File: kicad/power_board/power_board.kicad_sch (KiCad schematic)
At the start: 62 parts, among them J1 24V, J10 Grid, J11 24V Solar, J12 MCU_2, J13 GND, J2 24V, J3 GND, J4 GND, J5 GND, J6 GND, J7 MCU, J8 GND, J9 Solar Panel, Q1 FDD8453LZ, Q2 FDD8453LZ, Q3 FDD8453LZ, Q4 FDD8453LZ, Q5 FDS5670, U1 LTC4151xMS, U5 LT3757A, U6 LT1161

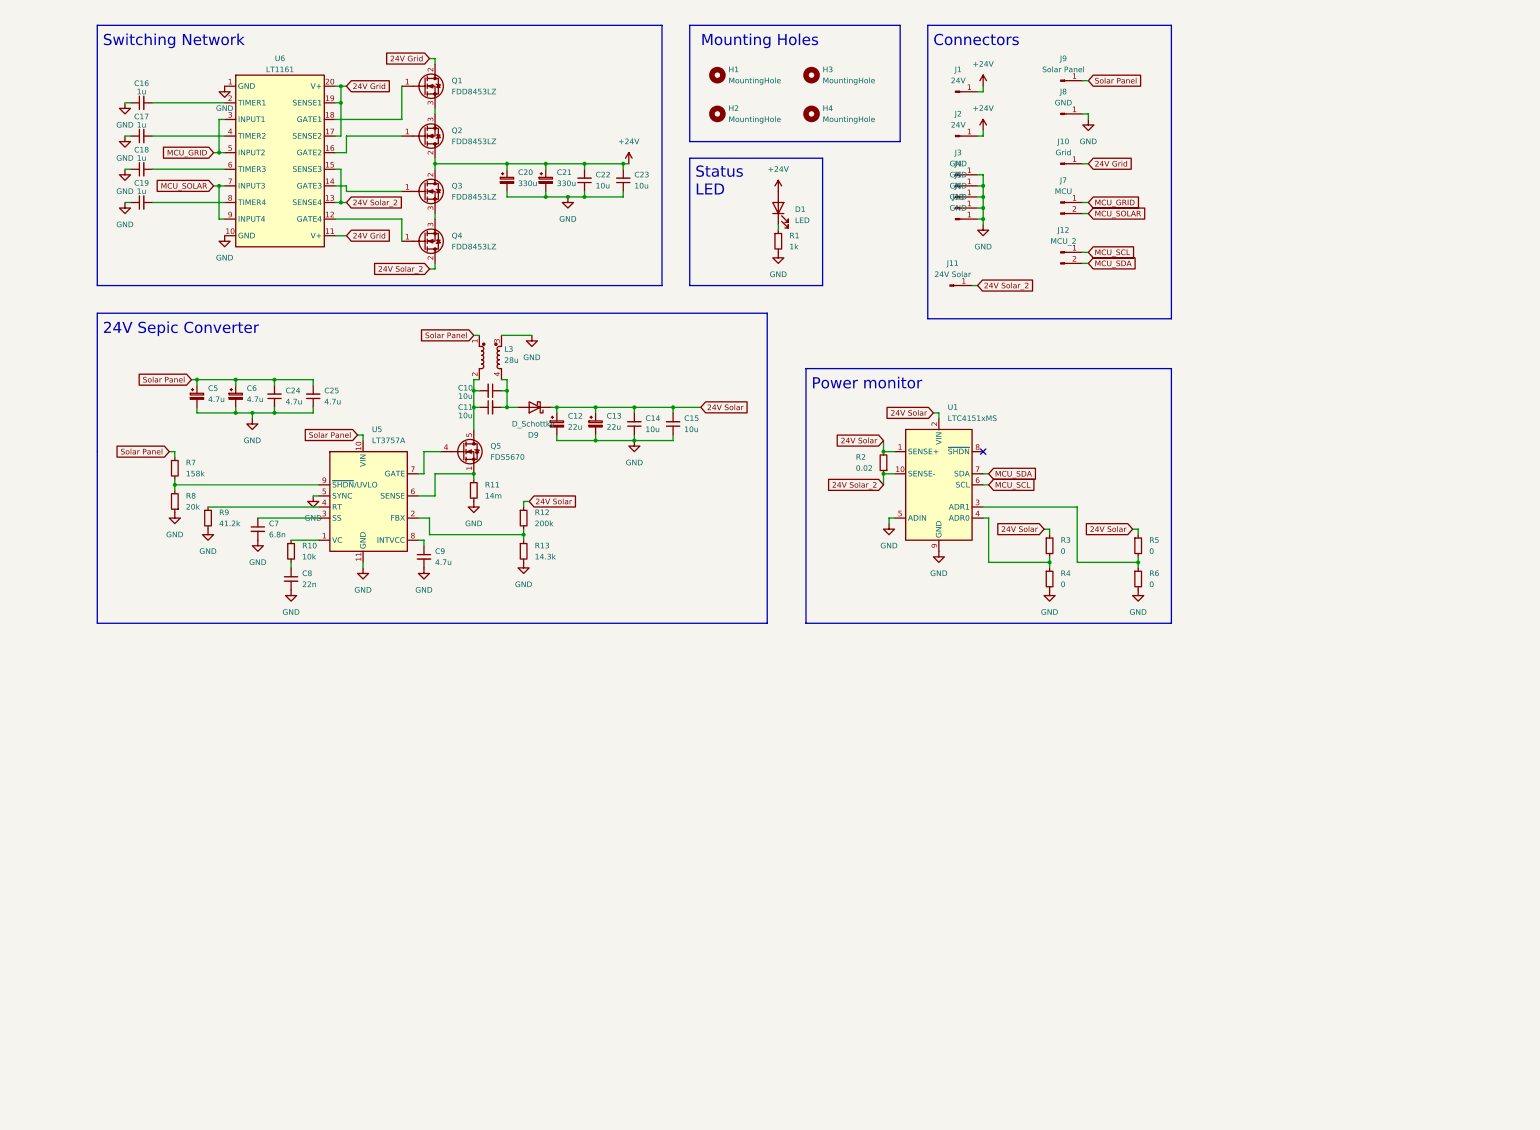
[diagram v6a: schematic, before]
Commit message: added isolation to power and light boards
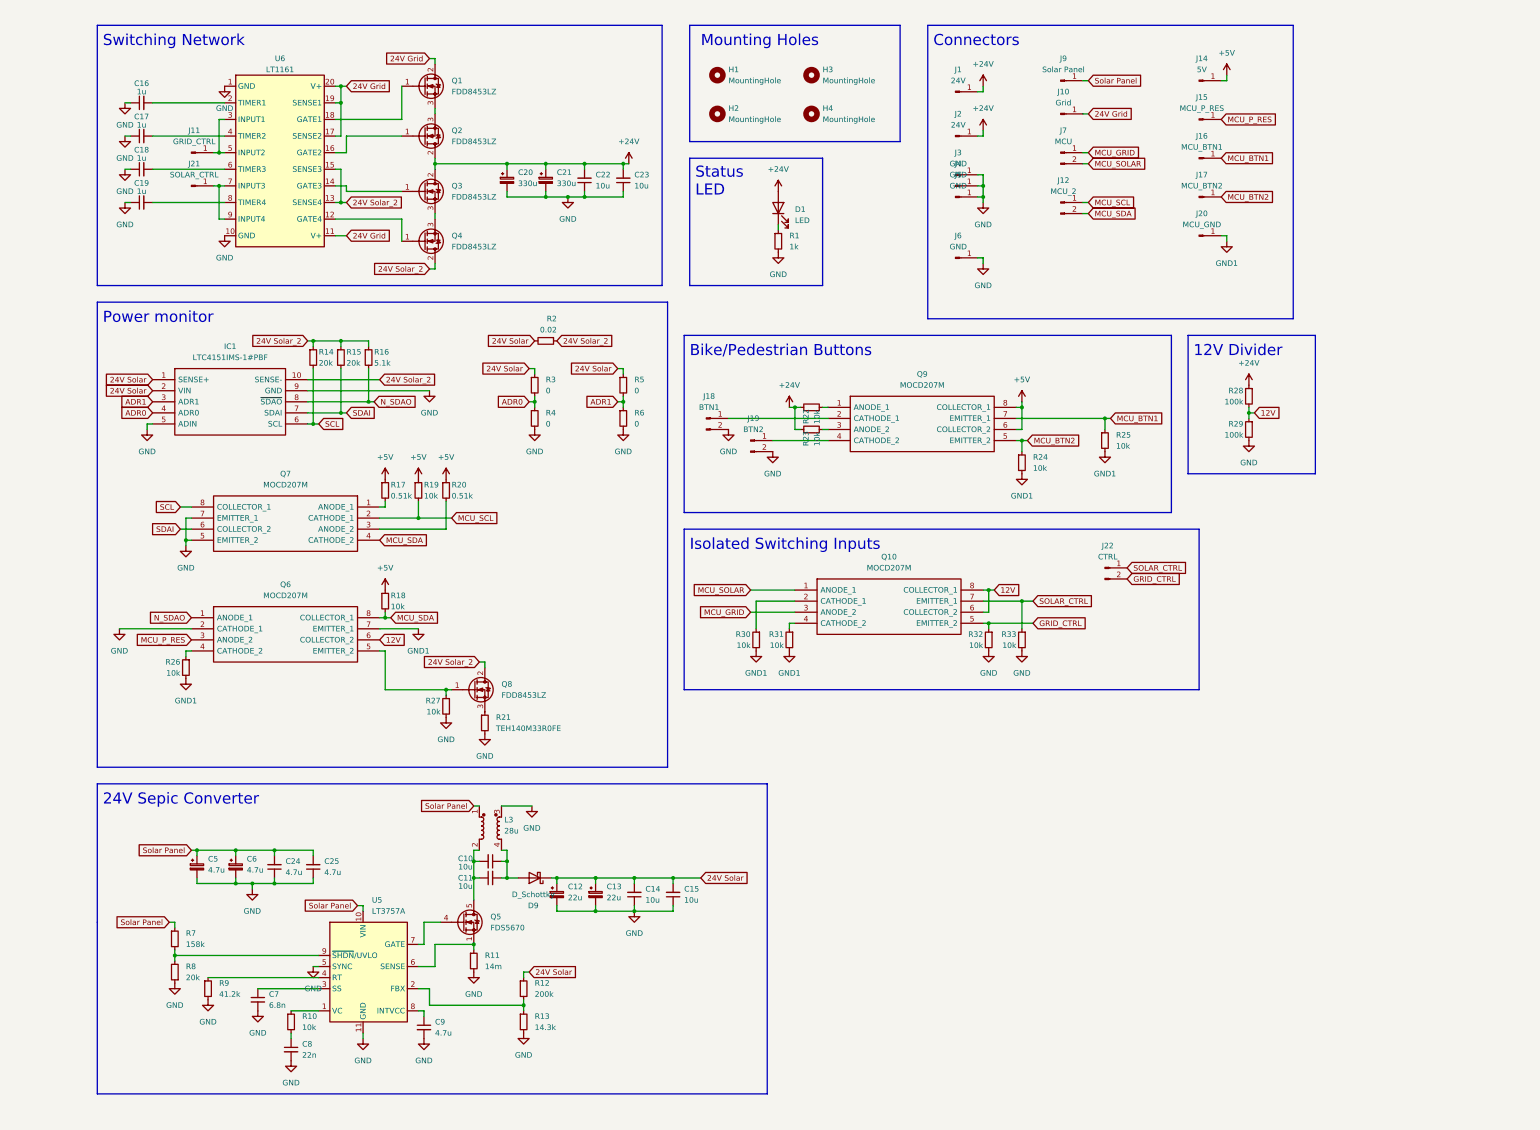
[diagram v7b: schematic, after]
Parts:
- removed J13: GND, Connector_PinHeader_2.54mm:PinHeader_1x01_P2.54mm_Vertical, symbol Connector:Conn_01x01_Male
- removed J8: GND, _mine:73099, symbol Connector:Conn_01x01_Male
- removed U1: LTC4151xMS, Package_SO:MSOP-10_3x3mm_P0.5mm, symbol Analog_ADC:LTC4151xMS
- added IC1: LTC4151IMS-1#PBF, Package_SO:MSOP-10_3x3mm_P0.5mm, symbol SamacSys_Parts:LTC4151IMS-1#PBF
- added J14: 5V, Connector_PinHeader_2.54mm:PinHeader_1x01_P2.54mm_Vertical, symbol Connector:Conn_01x01_Male
- added J15: MCU_P_RES, Connector_PinHeader_2.54mm:PinHeader_1x01_P2.54mm_Vertical, symbol Connector:Conn_01x01_Male
- added J16: MCU_BTN1, Connector_PinHeader_2.54mm:PinHeader_1x01_P2.54mm_Vertical, symbol Connector:Conn_01x01_Male
- added J17: MCU_BTN2, Connector_PinHeader_2.54mm:PinHeader_1x01_P2.54mm_Vertical, symbol Connector:Conn_01x01_Male
- added J18: BTN1, Connector_PinHeader_2.54mm:PinHeader_1x02_P2.54mm_Vertical, symbol Connector:Conn_01x02_Male
- added J19: BTN2, Connector_PinHeader_2.54mm:PinHeader_1x02_P2.54mm_Vertical, symbol Connector:Conn_01x02_Male
- added J20: MCU_GND, Connector_PinHeader_2.54mm:PinHeader_1x01_P2.54mm_Vertical, symbol Connector:Conn_01x01_Male
- added J21: SOLAR_CTRL, Connector_PinHeader_2.54mm:PinHeader_1x01_P2.54mm_Vertical, symbol Connector:Conn_01x01_Male
- added J22: CTRL, Connector_PinHeader_2.54mm:PinHeader_1x02_P2.54mm_Vertical, symbol Connector:Conn_01x02_Male
- added Q10, Q6, Q7, Q9: MOCD207M, Package_SO:SOIC-8_3.9x4.9mm_P1.27mm, symbol SamacSys_Parts:MOCD207M
- added Q8: FDD8453LZ, Package_TO_SOT_SMD:TO-252-2, symbol Transistor_FET:BSP89
- added R14, R15: 20k, Resistor_SMD:R_0603_1608Metric, symbol Device:R_Small
- added R16: 5.1k, Resistor_SMD:R_0603_1608Metric, symbol Device:R_Small
- added R17, R20: 0.51k, Resistor_SMD:R_0805_2012Metric, symbol Device:R_Small
- added R18, R19, R22, R23, R24, R25, R26, R27, R30, R31, R32, R33: 10k, Resistor_SMD:R_0805_2012Metric, symbol Device:R_Small
- added R21: TEH140M33R0FE, Resistor_THT:R_Axial_DIN0207_L6.3mm_D2.5mm_P10.16mm_Horizontal, symbol Device:R_Small
- added R28, R29: 100k, Resistor_SMD:R_1206_3216Metric, symbol Device:R_Small
- J11: value 24V Solar -> GRID_CTRL
- J6: footprint Connector_PinHeader_2.54mm:PinHeader_1x01_P2.54mm_Vertical -> _mine:73099
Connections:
- net +24V: now also R22.1, R23.1, R28.1
- net 24V Solar: now also IC1.1 (SENSE+), IC1.2 (VIN)
- net 24V Solar_2: now also IC1.10 (SENSE-), Q8.2 (D), R14.1, R15.1, R16.1; no longer J11.1 (Pin_1)
- net GND: now also IC1.5 (ADIN), IC1.9 (GND), J18.2 (Pin_2), J19.2 (Pin_2), Q6.2 (CATHODE_1), Q7.5 (EMITTER_2), Q7.7 (EMITTER_1), R21.2, R27.2, R29.2, R32.2, R33.2
- net MCU_GRID: now also Q10.3 (ANODE_2); no longer U6.3 (INPUT1), U6.5 (INPUT2)
- net MCU_SCL: now also Q7.2 (CATHODE_1), R19.2
- net MCU_SDA: now also Q6.8 (COLLECTOR_1), Q7.4 (CATHODE_2), R18.2
- net MCU_SOLAR: now also Q10.1 (ANODE_1); no longer U6.7 (INPUT3), U6.9 (INPUT4)
- net ADR0: now reaches R3.2, R4.1
- net ADR0: now also IC1.4 (ADR0)
- net ADR1: now reaches R5.2, R6.1
- net ADR1: now also IC1.3 (ADR1)
- new net: J11.1 (Pin_1), U6.3 (INPUT1), U6.5 (INPUT2)
- new net: Q7.1 (ANODE_1), R17.2
- new net: Q8.3 (S), R21.1
- new net: Q10.2 (CATHODE_1), R30.1
- new net: Q10.4 (CATHODE_2), R31.1
- new net: Q6.5 (EMITTER_2), Q8.1 (G), R27.1
- new net: Q7.3 (ANODE_2), R20.2
- new net: Q9.1 (ANODE_1), R22.2
- new net: J18.1 (Pin_1), Q9.2 (CATHODE_1)
- new net: Q9.3 (ANODE_2), R23.2
- new net: J19.1 (Pin_1), Q9.4 (CATHODE_2)
- new net: J21.1 (Pin_1), U6.7 (INPUT3), U6.9 (INPUT4)
- new net: Q6.4 (CATHODE_2), R26.1
- new net +5V: J14.1 (Pin_1), Q9.6 (COLLECTOR_2), Q9.8 (COLLECTOR_1), R17.1, R18.1, R19.1, R20.1
- new net 12V: Q10.6 (COLLECTOR_2), Q10.8 (COLLECTOR_1), Q6.6 (COLLECTOR_2), R28.2, R29.1
- new net GND1: J20.1 (Pin_1), Q6.7 (EMITTER_1), R24.2, R25.2, R26.2, R30.2, R31.2
- new net GRID_CTRL: J22.2 (Pin_2), Q10.5 (EMITTER_2), R32.1
- new net MCU_BTN1: J16.1 (Pin_1), Q9.7 (EMITTER_1), R25.1
- new net MCU_BTN2: J17.1 (Pin_1), Q9.5 (EMITTER_2), R24.1
- new net MCU_P_RES: J15.1 (Pin_1), Q6.3 (ANODE_2)
- new net N_SDAO: IC1.8 (~{SDAO}), Q6.1 (ANODE_1), R16.2
- new net SCL: IC1.6 (SCL), Q7.8 (COLLECTOR_1), R14.2
- new net SDAI: IC1.7 (SDAI), Q7.6 (COLLECTOR_2), R15.2
- new net SOLAR_CTRL: J22.1 (Pin_1), Q10.7 (EMITTER_1), R33.1
- no-connect marks 1 -> 0
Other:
- note added: "12V Divider"
- note added: "Bike/Pedestrian Buttons"
- note added: "Isolated Switching Inputs"
- moved on the sheet: C10, C11, C12, C13, C14, C15, C24, C25, C5, C6, C7, C8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

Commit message: update pcbs
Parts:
- removed C16, C17, C18, C19: 1u, Capacitor_SMD:C_0603_1608Metric, symbol Device:C_Small
- removed R28, R29: 100k, Resistor_SMD:R_1206_3216Metric, symbol Device:R_Small
- removed R3, R4, R5, R6: 0, Resistor_SMD:R_2512_6332Metric, symbol Device:R_Small
- added J13: GND, Connector_PinHeader_2.54mm:PinHeader_1x01_P2.54mm_Vertical, symbol Connector:Conn_01x01_Male
- added J23: 24V, _mylib:hole, symbol Connector:Conn_01x01_Male
- added J24: GND, _mylib:hole, symbol Connector:Conn_01x01_Male
- added J8: 5V_noisy, Connector_PinHeader_2.54mm:PinHeader_1x01_P2.54mm_Vertical, symbol Connector:Conn_01x01_Male
- added JP1, JP2, JP3, JP4, JP5, JP6, JP7, JP8, JP9: SolderJumper_2_Open, Jumper:SolderJumper-2_P1.3mm_Open_TrianglePad1.0x1.5mm, symbol Jumper:SolderJumper_2_Open
- C24, C25: footprint Capacitor_SMD:C_1210_3225Metric -> Capacitor_SMD:C_0805_2012Metric
- J10, J4: footprint Connector_PinHeader_2.54mm:PinHeader_1x01_P2.54mm_Vertical -> _mylib:hole
- J14: value 5V -> MCU_5V
- J6, J9: footprint _mine:73099 -> _mylib:hole_1.6mm
- Q5: footprint Package_TO_SOT_SMD:LFPAK33 -> Package_SO:SOIC-8_3.9x4.9mm_P1.27mm
- R1: footprint Resistor_SMD:R_2512_6332Metric -> Resistor_SMD:R_0603_1608Metric
- R14, R15: value 20k -> 10k
- R16: value 5.1k -> 2.4k
- R17, R20: value 0.51k -> 240; footprint Resistor_SMD:R_0805_2012Metric -> Resistor_SMD:R_0603_1608Metric
- R18, R19: value 10k -> 5.1k; footprint Resistor_SMD:R_0805_2012Metric -> Resistor_SMD:R_0603_1608Metric
- R21: footprint Resistor_THT:R_Axial_DIN0207_L6.3mm_D2.5mm_P10.16mm_Horizontal -> _mylib:TEH140
- R22, R23, R24, R25, R27, R32, R33: value 10k -> 1k; footprint Resistor_SMD:R_0805_2012Metric -> Resistor_SMD:R_0603_1608Metric
- R26, R30, R31: value 10k -> 150; footprint Resistor_SMD:R_0805_2012Metric -> Resistor_SMD:R_0603_1608Metric
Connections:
- net 12V is gone; now on net +5V: Q10.6 (COLLECTOR_2), Q10.8 (COLLECTOR_1), Q6.6 (COLLECTOR_2)
- net +24V: now also J23.1 (Pin_1)
- net +5V: now also J8.1 (Pin_1), JP8.2 (B); no longer J14.1 (Pin_1), Q9.6 (COLLECTOR_2), Q9.8 (COLLECTOR_1), R17.1, R18.1, R19.1, R20.1
- net 24V Solar: now also JP1.1 (A), JP3.1 (A)
- net 24V Solar_2: now also R21.1; no longer Q8.2 (D)
- net ADR0: now also JP1.2 (B), JP2.1 (A)
- net ADR1: now also JP3.2 (B), JP4.1 (A)
- net GND: now also L3.2, Q8.3 (S), J13.1 (Pin_1), J24.1 (Pin_1), JP2.2 (B), JP4.2 (B), JP9.1 (A); no longer L3.3, R21.2
- net GND1: now also JP9.2 (B)
- net GRID_CTRL: now also JP7.2 (B)
- net MCU_GRID: now also JP7.1 (A)
- net MCU_P_RES: now also JP5.1 (A)
- net MCU_SOLAR: now also JP6.1 (A)
- net SOLAR_CTRL: now also JP6.2 (B)
- net at Q6.5 (EMITTER_2), Q8.1 (G), R27.1: now also JP5.2 (B)
- net at C10.2, C11.1, Q5.5 (D): now also L3.3, Q5.6 (S), Q5.7 (S), Q5.8 (S); no longer L3.2
- new net: Q8.2 (D), R21.2
- new net MCU_5V: J14.1 (Pin_1), JP8.1 (A), Q9.6 (COLLECTOR_2), Q9.8 (COLLECTOR_1), R17.1, R18.1, R19.1, R20.1
- no-connect marks 0 -> 4
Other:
- note added: "5V Noisy"
- note added: "Grid Input"
- note added: "Isolated Bike/Pedestrian Buttons"
- note added: "Light Board"
- note added: "MCU Board"
- note added: "MCU/5V Buck Boards"
- note added: "Note: Probably don't need this one"
- note added: "Optional Jumpers"
- note added: "Solar Input"
- note removed: "12V Divider"
- note removed: "Bike/Pedestrian Buttons"
- moved on the sheet: C10, C11, C12, C13, C14, C15, C20, C21, C22, C23, C24, C25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
